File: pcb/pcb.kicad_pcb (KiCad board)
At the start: 2 copper layers, 21.6 x 12.7 mm, 0 parts

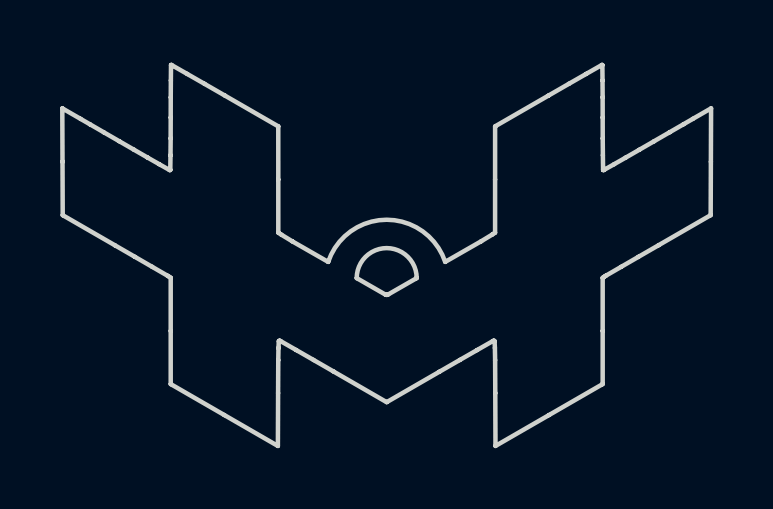
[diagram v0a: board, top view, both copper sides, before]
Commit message: Create and fill zones
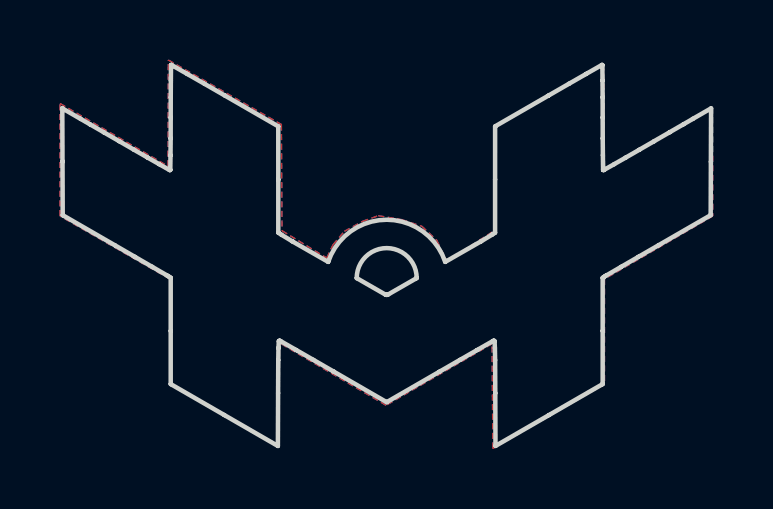
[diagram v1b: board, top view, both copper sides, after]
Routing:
- added copper zone on B.Cu, net (none)
- added copper zone on F.Cu, net (none)
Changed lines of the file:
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@@
     (solder_mask_min_width 0.25)
     (aux_axis_origin 0 0)
-    (visible_elements FFFFFF7F)
+    (visible_elements 7FFFFFFF)
     (pcbplotparams
       (layerselection 0x010fc_ffffffff)
@@
   (gr_line (start 151.299476 108.529909) (end 151.977459 108.13918) (layer Edge.Cuts) (width 0.15))
   (gr_line (start 147.78 108.53) (end 149.539735 109.545803) (layer Edge.Cuts) (width 0.15))
+  (zone (net 0) (net_name "") (layer F.Cu) (hatch edge 0.508)
+    (connect_pads (clearance 0.508))
+    (min_thickness 0.254)
+    (fill yes (arc_segments 32) (thermal_gap 0.508) (thermal_bridge_width 0.508))
+    (polygon
+      (pts
+        (xy 146.03 100.29) (xy 146.05 103.83) (xy 147.54 104.74) (xy 147.75 104.3) (xy 148.13 103.85)
+        (xy 148.73 103.52) (xy 149.26 103.33) (xy 150.04 103.46) (xy 150.71 103.68) (xy 151.21 104.15)
+        (xy 151.54 104.84) (xy 153.16 103.81) (xy 153.15 100.34) (xy 156.77 98.29) (xy 156.8 101.77)
+        (xy 160.4 99.73) (xy 160.41 103.34) (xy 156.8 105.44) (xy 156.8 108.95) (xy 153.08 111.09)
+        (xy 153.05 107.6) (xy 149.52 109.65) (xy 145.97 107.57) (xy 145.95 111.06) (xy 142.31 108.95)
+        (xy 142.31 105.44) (xy 138.65 103.34) (xy 138.65 99.59) (xy 142.25 101.68) (xy 142.26 98.14)
+      )
+    )
+  )
+  (zone (net 0) (net_name "") (layer B.Cu) (hatch edge 0.508)
+    (connect_pads (clearance 0.508))
+    (min_thickness 0.254)
+    (fill yes (arc_segments 32) (thermal_gap 0.508) (thermal_bridge_width 0.508))
+    (polygon
+      (pts
+        (xy 146.03 100.29) (xy 146.05 103.83) (xy 147.54 104.74) (xy 147.75 104.3) (xy 148.13 103.85)
+        (xy 148.73 103.52) (xy 149.26 103.33) (xy 150.04 103.46) (xy 150.71 103.68) (xy 151.21 104.15)
+        (xy 151.54 104.84) (xy 153.16 103.81) (xy 153.15 100.34) (xy 156.77 98.29) (xy 156.8 101.77)
+        (xy 160.4 99.73) (xy 160.41 103.34) (xy 156.8 105.44) (xy 156.8 108.95) (xy 153.08 111.09)
+        (xy 153.05 107.6) (xy 149.52 109.65) (xy 145.97 107.57) (xy 145.95 111.06) (xy 142.31 108.95)
+        (xy 142.31 105.44) (xy 138.65 103.34) (xy 138.65 99.59) (xy 142.25 101.68) (xy 142.26 98.14)
+      )
+    )
+  )
 )
